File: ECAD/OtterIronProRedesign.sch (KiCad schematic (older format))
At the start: 23 parts, among them J1 Conn_01x01, J2 Conn_01x01, J3 Conn_01x06, SW1 SW_Push, SW2 SW_Push

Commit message: routing almost done
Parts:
- removed C2: 470µF 35V, Capacitor_SMD:CP_Elec_10x10.5, symbol Device:CP
- removed J3: Conn_01x06, OtterIronPro_UiBoard:RPC1-12RB-6P(71), symbol Connector_Generic:Conn_01x06
- removed NT1, NT8: Net-Tie_2, NetTie:NetTie-2_SMD_Pad2.0mm, symbol Device:Net-Tie_2
- removed NT2, NT3, NT4, NT5, NT6, NT7: Net-Tie_2, NetTie:NetTie-2_SMD_Pad0.5mm, symbol Device:Net-Tie_2
- removed R5: Heater, symbol Device:Heater
- removed TC1: Thermocouple, symbol Device:Thermocouple
- added H1, H4: MountingHole, MountingHole:MountingHole_3.2mm_M3, symbol Mechanical:MountingHole
- added J1, J11, J12, J14, J16, J17, J19, J2, J4, J6, J8, J9: Conn_01x01, TestPoint:TestPoint_Pad_3.0x3.0mm, symbol Connector_Generic:Conn_01x01
- added J21: Conn_01x01, TestPoint:TestPoint_Keystone_5019_Minature, symbol OtterIronProRedesign-rescue:Conn_01x01-Connector_Generic
- added R6: 1M, Diode_SMD:D_0402_1005Metric, symbol Device:R
- C1: symbol Device:C -> OtterIronProRedesign-rescue:C-Device
- D1: value 30V 10A -> 24V 10A; symbol Device:D_Zener -> OtterIronProRedesign-rescue:D_Zener-Device; LCSC C133662 -> C284099; manf# SMBJ33A-TR -> SMBJ24CA
- F1: value 4A fast blowing -> 10A fast blowing; symbol Device:Fuse -> OtterIronProRedesign-rescue:Fuse-Device
- J20: renamed from J1; footprint Connector_Wire:SolderWire-0.5sqmm_1x01_D0.9mm_OD2.3mm -> TestPoint:TestPoint_Keystone_5019_Minature; symbol Connector_Generic:Conn_01x01 -> OtterIronProRedesign-rescue:Conn_01x01-Connector_Generic
- J22: renamed from J2; footprint Connector_Wire:SolderWire-0.5sqmm_1x01_D0.9mm_OD2.3mm -> TestPoint:TestPoint_Keystone_5019_Minature; symbol Connector_Generic:Conn_01x01 -> OtterIronProRedesign-rescue:Conn_01x01-Connector_Generic
- R1, R2: symbol Device:R -> OtterIronProRedesign-rescue:R-Device
- R4: renamed from R3; value 560k -> 68k; symbol Device:R -> OtterIronProRedesign-rescue:R-Device
- R5: renamed from R4; value R -> 10k; symbol Device:R -> OtterIronProRedesign-rescue:R-Device
- SW1, SW2: symbol Switch:SW_Push -> OtterIronProRedesign-rescue:SW_Push-Switch
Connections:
- wire segments 92 -> 69
- no-connect marks 3 -> 0
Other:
- note added: "TODO: larger display with same pinout?"
- note added: "TODO: pin for PwmL"
- note added: "power return for heater"
- note removed: "Pcb 1"
- note removed: "Pcb 2"
- note removed: "for illustration only"
- moved on the sheet: D1, F1, J20, J22, SW1, SW2

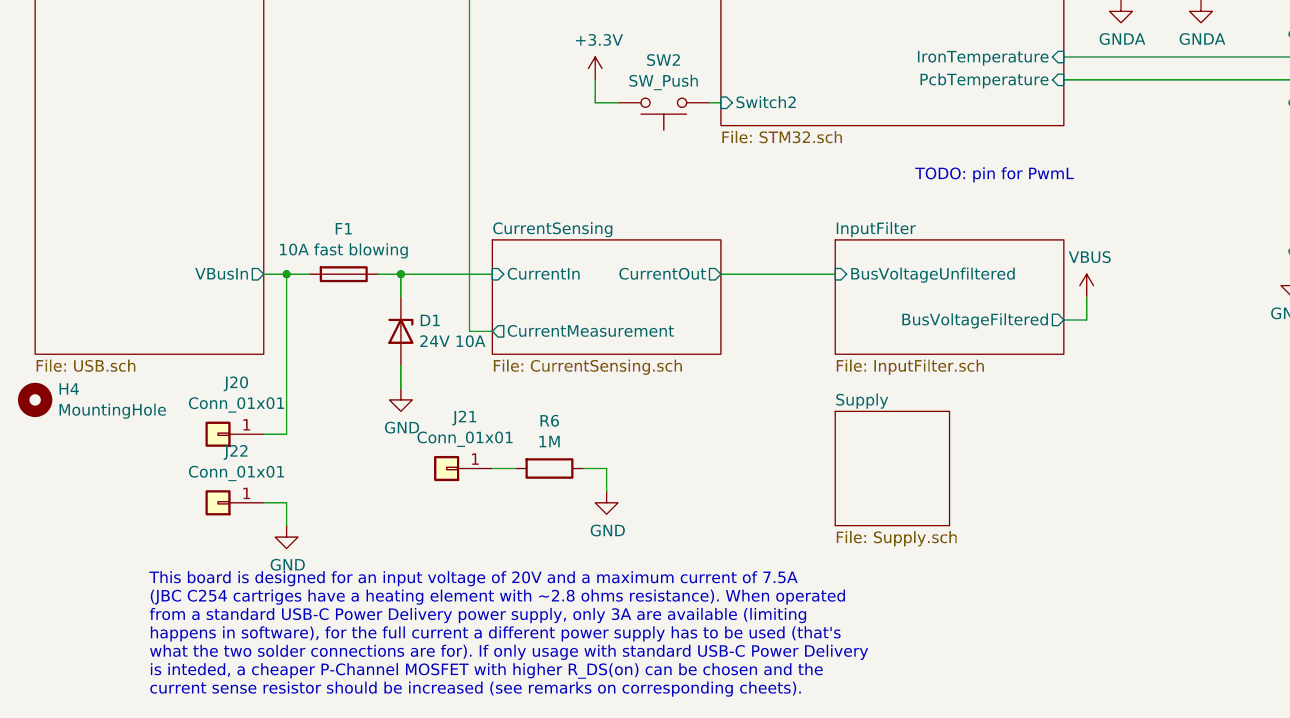
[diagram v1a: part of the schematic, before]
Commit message: swapped microcontroller
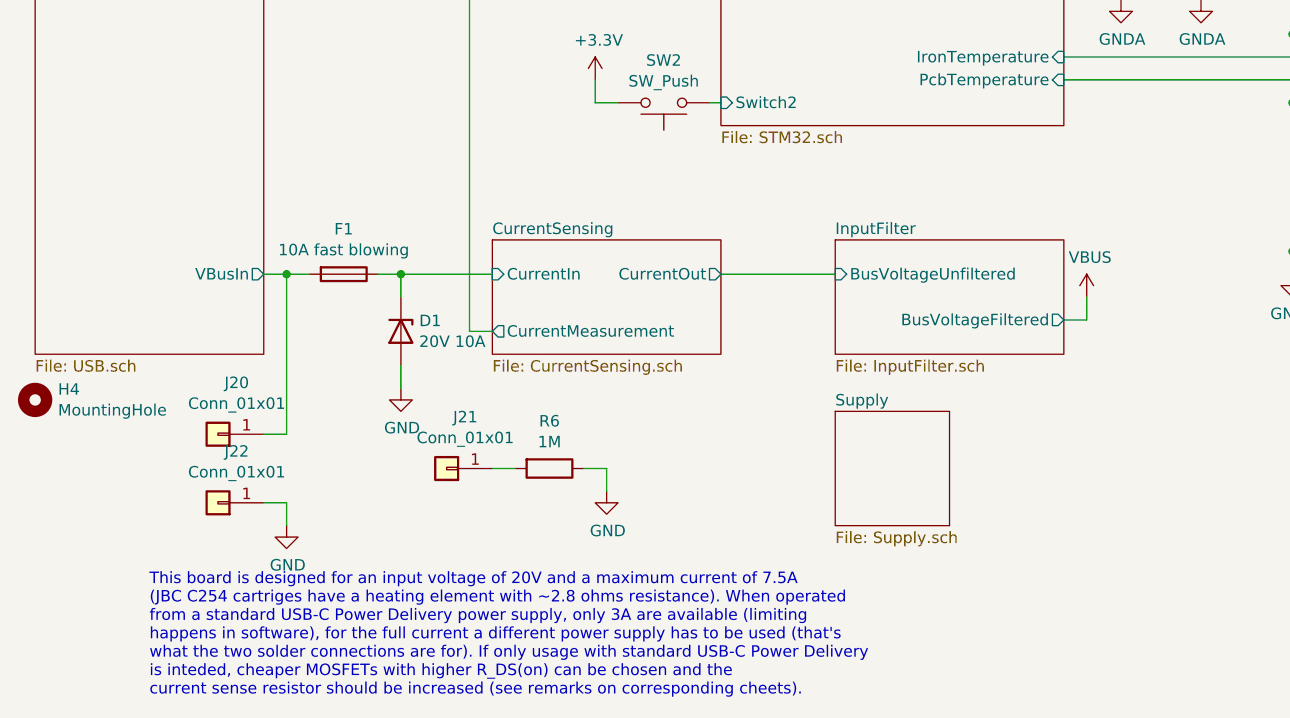
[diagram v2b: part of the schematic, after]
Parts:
- D1: value 24V 10A -> 20V 10A; LCSC C284099 -> C151257; manf# SMBJ24CA -> SMBJ20A
- R6: footprint Diode_SMD:D_0402_1005Metric -> Resistor_SMD:R_0402_1005Metric
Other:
- note removed: "TODO: pin for PwmL"
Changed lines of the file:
@@
 P 2600 5900
 F 0 "D1" V 2554 5980 50  0000 L CNN
-F 1 "24V 10A" V 2645 5980 50  0000 L CNN
+F 1 "20V 10A" V 2645 5980 50  0000 L CNN
 F 2 "Diode_SMD:D_SMB" H 2600 5900 50  0001 C CNN
 F 3 "~" H 2600 5900 50  0001 C CNN
-F 4 "SMBJ24CA" V 2600 5900 50  0001 C CNN "manf#"
-F 5 "C284099" V 2600 5900 50  0001 C CNN "LCSC"
+F 4 "SMBJ20A" V 2600 5900 50  0001 C CNN "manf#"
+F 5 "C151257" V 2600 5900 50  0001 C CNN "LCSC"
 	1    2600 5900
 	0    1    1    0
@@
 	5500 4100 5750 4100
 Text Notes 1500 7500 0    50   ~ 0
-This board is designed for an input voltage of 20V and a maximum current of 7.5A\n(JBC C254 cartriges have a heating element with ~~2.8 ohms resistance). When operated\nfrom a standard USB-C Power Delivery power supply, only 3A are available (limiting\nhappens in software), for the full current a different power supply has to be used (that's\nwhat the two solder connections are for). If only usage with standard USB-C Power Delivery\nis inteded, a cheaper P-Channel MOSFET with higher R_DS(on) can be chosen and the\ncurrent sense resistor should be increased (see remarks on corresponding cheets).
+This board is designed for an input voltage of 20V and a maximum current of 7.5A\n(JBC C254 cartriges have a heating element with ~~2.8 ohms resistance). When operated\nfrom a standard USB-C Power Delivery power supply, only 3A are available (limiting\nhappens in software), for the full current a different power supply has to be used (that's\nwhat the two solder connections are for). If only usage with standard USB-C Power Delivery\nis inteded, cheaper MOSFETs with higher R_DS(on) can be chosen and the\ncurrent sense resistor should be increased (see remarks on corresponding cheets).
 Wire Wire Line
 	5500 3200 6000 3200
 Wire Wire Line
 	5500 3300 6000 3300
-Text Notes 4850 5250 0    50   ~ 0
-TODO: pin for PwmL
 Text Notes 5900 1650 0    50   ~ 0
 TODO: larger display with same pinout?
@@
 F 0 "R6" V 3043 6500 50  0000 C CNN
 F 1 "1M" V 3134 6500 50  0000 C CNN
-F 2 "Diode_SMD:D_0402_1005Metric" V 3180 6500 50  0001 C CNN
+F 2 "Resistor_SMD:R_0402_1005Metric" V 3180 6500 50  0001 C CNN
 F 3 "~" H 3250 6500 50  0001 C CNN
 	1    3250 6500

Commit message: more routing + some component changes
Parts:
- added J3: Conn_01x01, TestPoint:TestPoint_Keystone_5019_Minature, symbol OtterIronProRedesign-rescue:Conn_01x01-Connector_Generic
- added R5: 1M, Resistor_SMD:R_0402_1005Metric, symbol Device:R
- added SW2: SW_Push, Button_Switch_SMD:SW_Push_1P1T_NO_6x6mm_H9.5mm, symbol OtterIronProRedesign-rescue:SW_Push-Switch
- D1: LCSC C151257 -> C309948
- F1: LCSC C163127 -> C182976; manf# CFS12V3T4R0 -> 12D2150E
- renumbered H4 to H2, J20 to J1, J16 to J10, J17 to J11, J19 to J12, J1 to J13, J2 to J14, J4 to J15, J6 to J16, J22 to J2, J21 to J4, J8 to J5, J9 to J6, J11 to J7, J12 to J8, J14 to J9, R4 to R3, R5 to R4, SW2 to SW3
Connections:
- net +3V3: now also R5.1
- new net: J3.1 (Pin_1), R5.2
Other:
- note added: "Extended parts:\nUSB-PD IC\nUSB TVS\nFuse\nTVS\nCurrent Amplifier\nCurrent Shunt\nSTM32\nFilter Inductor\nFilter Capacitor\nGate Driver\nMOSFETs\n9V Regulator\n3.3V Regulator"
- note removed: "TODO: larger display with same pinout?"
- moved on the sheet: J4, R6
